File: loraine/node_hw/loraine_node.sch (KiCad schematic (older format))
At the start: 36 parts

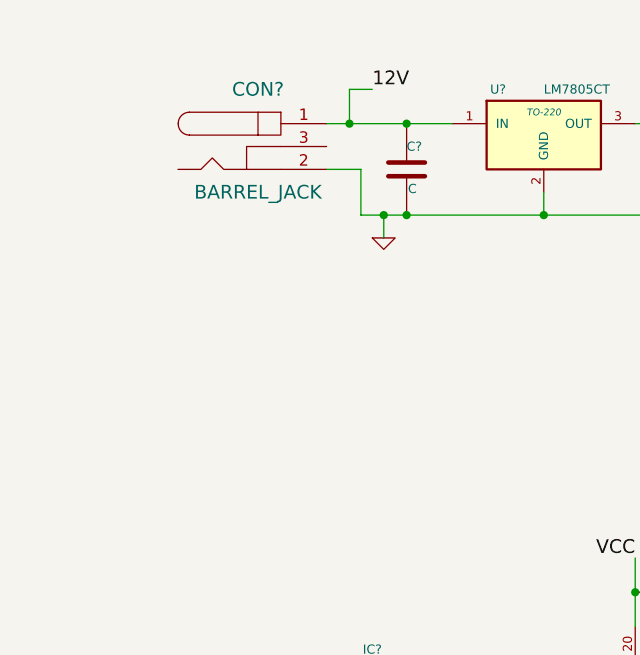
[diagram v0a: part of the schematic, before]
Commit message: Added extra power connectors
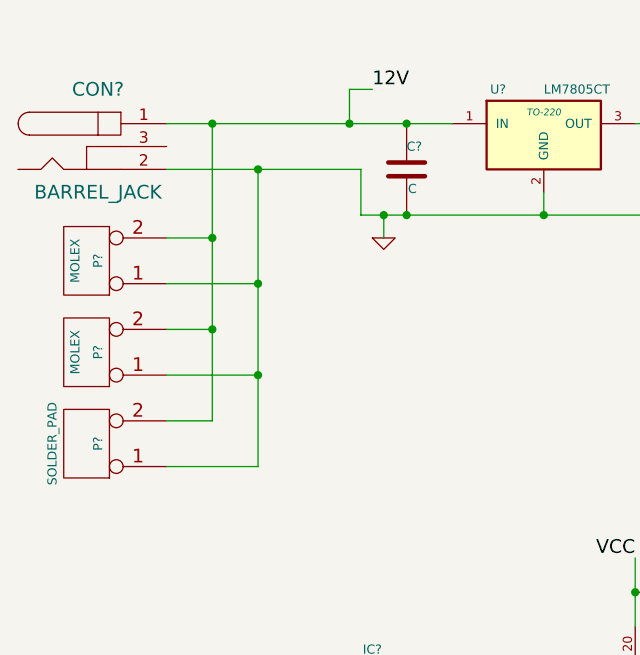
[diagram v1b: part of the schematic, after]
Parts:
- added P? (x2): MOLEX, symbol CONN_2
- added P?: SOLDER_PAD, symbol CONN_2
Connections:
- net 12V: now also P?.2 (PM), P?.2 (PM), P?.2 (PM)
- net GND: now also P?.1 (P1), P?.1 (P1), P?.1 (P1)
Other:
- moved on the sheet: CON?
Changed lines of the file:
@@
 L BARREL_JACK CON?
 U 1 1 533879A3
-P 1800 1250
-F 0 "CON?" H 1800 1500 60  0000 C CNN
-F 1 "BARREL_JACK" H 1800 1050 60  0000 C CNN
-F 2 "" H 1800 1250 60  0000 C CNN
-F 3 "" H 1800 1250 60  0000 C CNN
-	1    1800 1250
+P 1100 1250
+F 0 "CON?" H 1100 1500 60  0000 C CNN
+F 1 "BARREL_JACK" H 1100 1050 60  0000 C CNN
+F 2 "" H 1100 1250 60  0000 C CNN
+F 3 "" H 1100 1250 60  0000 C CNN
+	1    1100 1250
 	1    0    0    -1
 $EndComp
@@
 	3450 1150 4150 1150
 Wire Wire Line
-	2100 1150 2650 1150
-Wire Wire Line
-	2100 1350 2250 1350
+	1400 1150 2650 1150
+Wire Wire Line
+	1400 1350 2250 1350
 Wire Wire Line
 	2250 1350 2250 1550
@@
 Wire Wire Line
 	3850 3200 3850 3350
+$Comp
+L CONN_2 P?
+U 1 1 5338B71A
+P 1050 1750
+F 0 "P?" V 1000 1750 40  0000 C CNN
+F 1 "MOLEX" V 1100 1750 40  0000 C CNN
+F 2 "" H 1050 1750 60  0000 C CNN
+F 3 "" H 1050 1750 60  0000 C CNN
+	1    1050 1750
+	-1   0    0    1
+$EndComp
+$Comp
+L CONN_2 P?
+U 1 1 5338B738
+P 1050 2150
+F 0 "P?" V 1000 2150 40  0000 C CNN
+F 1 "MOLEX" V 1100 2150 40  0000 C CNN
+F 2 "" H 1050 2150 60  0000 C CNN
+F 3 "" H 1050 2150 60  0000 C CNN
+	1    1050 2150
+	-1   0    0    1
+$EndComp
+Wire Wire Line
+	1600 1150 1600 2450
+Connection ~ 1600 1150
+Wire Wire Line
+	1600 2050 1400 2050
+Wire Wire Line
+	1400 1650 1600 1650
+Connection ~ 1600 1650
+Wire Wire Line
+	1400 1850 1800 1850
+Wire Wire Line
+	1800 1350 1800 2650
+Connection ~ 1800 1350
+Wire Wire Line
+	1800 2250 1400 2250
+Connection ~ 1800 1850
+$Comp
+L CONN_2 P?
+U 1 1 5338BC50
+P 1050 2550
+F 0 "P?" V 1000 2550 40  0000 C CNN
+F 1 "SOLDER_PAD" V 1200 2550 40  0000 C CNN
+F 2 "" H 1050 2550 60  0000 C CNN
+F 3 "" H 1050 2550 60  0000 C CNN
+	1    1050 2550
+	-1   0    0    1
+$EndComp
+Wire Wire Line
+	1600 2450 1400 2450
+Connection ~ 1600 2050
+Wire Wire Line
+	1800 2650 1400 2650
+Connection ~ 1800 2250
 $EndSCHEMATC

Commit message: Added ICSP header
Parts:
- added P?: ICSP, symbol CONN_3X2
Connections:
- net GND: now also P?.6
- net VCC: now also P?.2
- net RESET: now reaches IC?.1 (PA2(~RESET~/dW/PCINT10))
- net RESET: now also P?.5
- net MOSI: now reaches IC?.17 ((PCINT5/MOSI/DI/SDA)PB5), R?.2
- net MOSI: now also P?.4
- net MISO: now reaches IC?.18 ((PCINT6/MISO/DO)PB6), R?.2
- net MISO: now also P?.1
- net SCK: now reaches IC?.19 ((PCINT7/USCK/SCK/SCL)PB7), R?.2
- net SCK: now also P?.3
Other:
- moved on the sheet: D?, P?, Q?, R?

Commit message: Added common anodes to outputs connector
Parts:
- removed P?: CONN_8, symbol CONN_8
- added P?: OUTPUTS, symbol CONN_8X2
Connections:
- net 12V: now also P?.10, P?.12, P?.14, P?.16, P?.2, P?.4, P?.6, P?.8
- net at D?.2 (K), Q?.3: now also P?.1
- net at D?.2 (K), Q?.3: now also P?.3
- net at D?.2 (K), Q?.3: now also P?.5
- net at Q?.3: now also P?.7
- net at Q?.3: now also P?.9
- net at Q?.3: now also P?.11
- net at Q?.3: now also P?.13
- net at Q?.3: now also P?.15
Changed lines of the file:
@@
 $EndComp
 Connection ~ 7000 6000
-$Comp
-L CONN_8 P?
-U 1 1 533887C0
-P 10950 5250
-F 0 "P?" V 10900 5250 60  0000 C CNN
-F 1 "CONN_8" V 11000 5250 60  0000 C CNN
-F 2 "" H 10950 5250 60  0000 C CNN
-F 3 "" H 10950 5250 60  0000 C CNN
-	1    10950 5250
-	1    0    0    -1
-$EndComp
 Text Label 3450 3050 2    60   ~ 0
 VCC
@@
 	3000 7150 3200 7150
 Wire Wire Line
-	6900 5600 10600 5600
-Wire Wire Line
-	7350 5500 10600 5500
-Wire Wire Line
-	7450 5400 10600 5400
-Wire Wire Line
 	6900 5100 7350 5100
 Wire Wire Line
-	7350 5100 7350 5500
-Wire Wire Line
-	7450 5400 7450 4600
-Wire Wire Line
 	7450 4600 6900 4600
 Wire Wire Line
@@
 Wire Wire Line
 	7950 2100 7950 4900
-Wire Wire Line
-	7550 5300 10600 5300
-Wire Wire Line
-	7650 5200 10600 5200
-Wire Wire Line
-	7750 5100 10600 5100
-Wire Wire Line
-	7850 5000 10600 5000
-Wire Wire Line
-	7950 4900 10600 4900
 $Comp
 L LED D?
@@
 Wire Wire Line
 	1950 3650 2100 3650
+$Comp
+L CONN_8X2 P?
+U 1 1 5338D875
+P 10050 5250
+F 0 "P?" H 10050 5700 60  0000 C CNN
+F 1 "OUTPUTS" V 10050 5250 50  0000 C CNN
+F 2 "" H 10050 5250 60  0000 C CNN
+F 3 "" H 10050 5250 60  0000 C CNN
+	1    10050 5250
+	1    0    0    -1
+$EndComp
+Wire Wire Line
+	6900 5600 9650 5600
+Wire Wire Line
+	7350 5100 7350 5500
+Wire Wire Line
+	7350 5500 9650 5500
+Wire Wire Line
+	7450 4600 7450 5400
+Wire Wire Line
+	7450 5400 9650 5400
+Wire Wire Line
+	7550 5300 9650 5300
+Wire Wire Line
+	7650 5200 9650 5200
+Wire Wire Line
+	7750 5100 9650 5100
+Wire Wire Line
+	7850 5000 9650 5000
+Wire Wire Line
+	7950 4900 9650 4900
+Text Label 10600 4800 0    60   ~ 0
+12V
+Wire Wire Line
+	10600 4800 10600 5600
+Wire Wire Line
+	10600 4900 10450 4900
+Wire Wire Line
+	10600 5000 10450 5000
+Connection ~ 10600 4900
+Wire Wire Line
+	10600 5100 10450 5100
+Connection ~ 10600 5000
+Wire Wire Line
+	10600 5200 10450 5200
+Connection ~ 10600 5100
+Wire Wire Line
+	10600 5300 10450 5300
+Connection ~ 10600 5200
+Wire Wire Line
+	10600 5400 10450 5400
+Connection ~ 10600 5300
+Wire Wire Line
+	10450 5500 10600 5500
+Connection ~ 10600 5400
+Wire Wire Line
+	10600 5600 10450 5600
+Connection ~ 10600 5500
 $EndSCHEMATC

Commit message: Filled in most component values
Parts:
- removed C? (x2): C, symbol C
- added C?: 0.33uF, symbol CP1
- C? (x2): value C -> 16pF
- C?: value CP1 -> 0.1uF
- C? (x2): value C -> 0.1u
- D?: value LED -> RED
- D?: value LED -> GREEN
- D?: value LED -> BLUE
- P?: value CONN_2 -> BUS
- R? (x8): value R -> 1k
- U?: value LM7805CT -> UA7805CKCT
- X?: value CRYSTAL -> 16MHz
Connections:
- net 12V: now also C?.1
- net GND: now also C?.2
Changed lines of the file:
@@
 P 3050 1200
 F 0 "U?" H 2850 1400 40  0000 C CNN
-F 1 "LM7805CT" H 3050 1400 40  0000 L CNN
+F 1 "UA7805CKCT" H 3050 1400 40  0000 L CNN
 F 2 "TO-220" H 3050 1300 30  0000 C CIN
 F 3 "" H 3050 1200 60  0000 C CNN
@@
 P 1800 4250
 F 0 "X?" H 1800 4400 60  0000 C CNN
-F 1 "CRYSTAL" H 1800 4100 60  0000 C CNN
+F 1 "16MHz" H 1800 4100 60  0000 C CNN
 F 2 "" H 1800 4250 60  0000 C CNN
 F 3 "" H 1800 4250 60  0000 C CNN
@@
 P 5850 3650
 F 0 "R?" V 5800 3850 40  0000 C CNN
-F 1 "R" V 5857 3651 40  0000 C CNN
+F 1 "1k" V 5857 3651 40  0000 C CNN
 F 2 "" V 5780 3650 30  0000 C CNN
 F 3 "" H 5850 3650 30  0000 C CNN
@@
 P 1450 4550
 F 0 "C?" H 1450 4650 40  0000 L CNN
-F 1 "C" H 1456 4465 40  0000 L CNN
+F 1 "16pF" H 1456 4465 40  0000 L CNN
 F 2 "" H 1488 4400 30  0000 C CNN
 F 3 "" H 1450 4550 60  0000 C CNN
@@
 P 1450 3950
 F 0 "C?" H 1450 4050 40  0000 L CNN
-F 1 "C" H 1456 3865 40  0000 L CNN
+F 1 "16pF" H 1456 3865 40  0000 L CNN
 F 2 "" H 1488 3800 30  0000 C CNN
 F 3 "" H 1450 3950 60  0000 C CNN
@@
 Text Label 2300 1000 0    60   ~ 0
 12V
-Text Label 4150 1550 0    60   ~ 0
+Text Label 3850 1550 0    60   ~ 0
 GND
 $Comp
@@
 	1    0    0    -1
 $EndComp
-Text Label 4150 1150 0    60   ~ 0
+Text Label 3850 1150 0    60   ~ 0
 VCC
-$Comp
-L C C?
-U 1 1 53387A28
-P 2450 1350
-F 0 "C?" H 2450 1450 40  0000 L CNN
-F 1 "C" H 2456 1265 40  0000 L CNN
-F 2 "" H 2488 1200 30  0000 C CNN
-F 3 "" H 2450 1350 60  0000 C CNN
-	1    2450 1350
-	1    0    0    -1
-$EndComp
 $Comp
 L CP1 C?
@@
 P 3600 1350
 F 0 "C?" H 3650 1450 50  0000 L CNN
-F 1 "CP1" H 3650 1250 50  0000 L CNN
+F 1 "0.1uF" H 3650 1250 50  0000 L CNN
 F 2 "" H 3600 1350 60  0000 C CNN
 F 3 "" H 3600 1350 60  0000 C CNN
@@
 	1    0    0    -1
 $EndComp
-Connection ~ 2450 1150
 Wire Wire Line
 	3050 1550 3050 1450
-Connection ~ 2450 1550
 Wire Wire Line
 	2350 1550 2350 1650
@@
 Connection ~ 3600 1150
 Connection ~ 3050 1550
-$Comp
-L C C?
-U 1 1 53387D68
-P 3900 1350
-F 0 "C?" H 3900 1450 40  0000 L CNN
-F 1 "C" H 3906 1265 40  0000 L CNN
-F 2 "" H 3938 1200 30  0000 C CNN
-F 3 "" H 3900 1350 60  0000 C CNN
-	1    3900 1350
-	1    0    0    -1
-$EndComp
-Connection ~ 3900 1150
 Connection ~ 3600 1550
-Wire Wire Line
-	2250 1550 4150 1550
-Connection ~ 3900 1550
-Wire Wire Line
-	3450 1150 4150 1150
-Wire Wire Line
-	1400 1150 2650 1150
 Wire Wire Line
 	1400 1350 2250 1350
@@
 P 5850 3750
 F 0 "R?" V 5800 3950 40  0000 C CNN
-F 1 "R" V 5857 3751 40  0000 C CNN
+F 1 "1k" V 5857 3751 40  0000 C CNN
 F 2 "" V 5780 3750 30  0000 C CNN
 F 3 "" H 5850 3750 30  0000 C CNN
@@
 P 5850 3850
 F 0 "R?" V 5800 4050 40  0000 C CNN
-F 1 "R" V 5857 3851 40  0000 C CNN
+F 1 "1k" V 5857 3851 40  0000 C CNN
 F 2 "" V 5780 3850 30  0000 C CNN
 F 3 "" H 5850 3850 30  0000 C CNN
@@
 P 5850 3950
 F 0 "R?" V 5800 4150 40  0000 C CNN
-F 1 "R" V 5857 3951 40  0000 C CNN
+F 1 "1k" V 5857 3951 40  0000 C CNN
 F 2 "" V 5780 3950 30  0000 C CNN
 F 3 "" H 5850 3950 30  0000 C CNN
@@
 P 5850 4050
 F 0 "R?" V 5800 4250 40  0000 C CNN
-F 1 "R" V 5857 4051 40  0000 C CNN
+F 1 "1k" V 5857 4051 40  0000 C CNN
 F 2 "" V 5780 4050 30  0000 C CNN
 F 3 "" H 5850 4050 30  0000 C CNN
@@
 P 5850 4150
 F 0 "R?" V 5800 4350 40  0000 C CNN
-F 1 "R" V 5857 4151 40  0000 C CNN
+F 1 "1k" V 5857 4151 40  0000 C CNN
 F 2 "" V 5780 4150 30  0000 C CNN
 F 3 "" H 5850 4150 30  0000 C CNN
@@
 P 5850 4250
 F 0 "R?" V 5800 4450 40  0000 C CNN
-F 1 "R" V 5857 4251 40  0000 C CNN
+F 1 "1k" V 5857 4251 40  0000 C CNN
 F 2 "" V 5780 4250 30  0000 C CNN
 F 3 "" H 5850 4250 30  0000 C CNN
@@
 P 5850 4350
 F 0 "R?" V 5800 4550 40  0000 C CNN
-F 1 "R" V 5857 4351 40  0000 C CNN
+F 1 "1k" V 5857 4351 40  0000 C CNN
 F 2 "" V 5780 4350 30  0000 C CNN
 F 3 "" H 5850 4350 30  0000 C CNN
@@
 Text Label 3450 3050 2    60   ~ 0
 VCC
-Text Label 3650 5450 2    60   ~ 0
-GND
 $Comp
 L ATTINY2313A-S IC?
@@
 $EndComp
 Wire Wire Line
-	3450 5450 3650 5450
-Wire Wire Line
 	4450 7000 4750 7000
 Wire Wire Line
@@
 P 2650 7050
 F 0 "P?" V 2600 7050 40  0000 C CNN
-F 1 "CONN_2" V 2700 7050 40  0000 C CNN
+F 1 "BUS" V 2700 7050 40  0000 C CNN
 F 2 "" H 2650 7050 60  0000 C CNN
 F 3 "" H 2650 7050 60  0000 C CNN
@@
 P 9050 1800
 F 0 "D?" H 9050 1900 50  0000 C CNN
-F 1 "LED" H 9050 1700 50  0000 C CNN
+F 1 "RED" H 9050 1700 50  0000 C CNN
 F 2 "" H 9050 1800 60  0000 C CNN
 F 3 "" H 9050 1800 60  0000 C CNN
@@
 P 9450 1800
 F 0 "D?" H 9450 1900 50  0000 C CNN
-F 1 "LED" H 9450 1700 50  0000 C CNN
+F 1 "GREEN" H 9400 1700 50  0000 C CNN
 F 2 "" H 9450 1800 60  0000 C CNN
 F 3 "" H 9450 1800 60  0000 C CNN
@@
 P 9850 1800
 F 0 "D?" H 9850 1900 50  0000 C CNN
-F 1 "LED" H 9850 1700 50  0000 C CNN
+F 1 "BLUE" H 9850 1700 50  0000 C CNN
 F 2 "" H 9850 1800 60  0000 C CNN
 F 3 "" H 9850 1800 60  0000 C CNN
@@
 U 1 1 5338A896
 P 2300 7050
-F 0 "C?" H 2300 7150 40  0000 L CNN
-F 1 "C" H 2306 6965 40  0000 L CNN
+F 0 "C?" H 2350 7150 40  0000 L CNN
+F 1 "0.1u" H 2340 6950 40  0000 L CNN
 F 2 "" H 2338 6900 30  0000 C CNN
 F 3 "" H 2300 7050 60  0000 C CNN
@@
 U 1 1 5338AB56
 P 3650 3200
-F 0 "C?" H 3650 3300 40  0000 L CNN
-F 1 "C" H 3656 3115 40  0000 L CNN
+F 0 "C?" V 3600 3250 40  0000 L CNN
+F 1 "0.1u" V 3710 3020 40  0000 L CNN
 F 2 "" H 3688 3050 30  0000 C CNN
 F 3 "" H 3650 3200 60  0000 C CNN
@@
 	10600 5600 10450 5600
 Connection ~ 10600 5500
+$Comp
+L CP1 C?
+U 1 1 5338EB5B
+P 2450 1350
+F 0 "C?" H 2500 1450 50  0000 L CNN
+F 1 "0.33uF" H 2500 1250 50  0000 L CNN
+F 2 "" H 2450 1350 60  0000 C CNN
+F 3 "" H 2450 1350 60  0000 C CNN
+	1    2450 1350
+	1    0    0    -1
+$EndComp
+Wire Wire Line
+	1400 1150 2650 1150
+Connection ~ 2450 1150
+Connection ~ 2450 1550
+Wire Wire Line
+	2250 1550 3850 1550
+Wire Wire Line
+	3450 1150 3850 1150
+$Comp
+L GND #PWR?
+U 1 1 5338F7A1
+P 3450 5500
+F 0 "#PWR?" H 3450 5500 30  0001 C CNN
+F 1 "GND" H 3450 5430 30  0001 C CNN
+F 2 "" H 3450 5500 60  0000 C CNN
+F 3 "" H 3450 5500 60  0000 C CNN
+	1    3450 5500
+	1    0    0    -1
+$EndComp
+Wire Wire Line
+	3450 5450 3450 5500
 $EndSCHEMATC

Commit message: Replaced VCC/GND labels with symbols
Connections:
- net VCC: no longer R?.1, R?.1, R?.1
- net 12V renamed +12V
- net +12V: now also R?.1, R?.1, R?.1
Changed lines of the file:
@@
 	1    0    0    -1
 $EndComp
-Text Label 2300 1000 0    60   ~ 0
-12V
-Text Label 3850 1550 0    60   ~ 0
-GND
 $Comp
 L GND #PWR?
 U 1 1 533879F1
-P 2350 1650
-F 0 "#PWR?" H 2350 1650 30  0001 C CNN
-F 1 "GND" H 2350 1580 30  0001 C CNN
-F 2 "" H 2350 1650 60  0000 C CNN
-F 3 "" H 2350 1650 60  0000 C CNN
-	1    2350 1650
-	1    0    0    -1
-$EndComp
-Text Label 3850 1150 0    60   ~ 0
-VCC
+P 3850 1650
+F 0 "#PWR?" H 3850 1650 30  0001 C CNN
+F 1 "GND" H 3850 1580 30  0001 C CNN
+F 2 "" H 3850 1650 60  0000 C CNN
+F 3 "" H 3850 1650 60  0000 C CNN
+	1    3850 1650
+	1    0    0    -1
+$EndComp
 $Comp
 L CP1 C?
@@
 Wire Wire Line
 	3050 1550 3050 1450
-Wire Wire Line
-	2350 1550 2350 1650
-Connection ~ 2350 1550
 Connection ~ 3600 1150
 Connection ~ 3050 1550
@@
 Wire Wire Line
 	2250 1350 2250 1550
-Wire Wire Line
-	2200 1000 2300 1000
 Connection ~ 2200 1150
-Wire Wire Line
-	2200 1150 2200 1000
 $Comp
 L R R?
@@
 $EndComp
 Connection ~ 7000 6000
-Text Label 3450 3050 2    60   ~ 0
-VCC
 $Comp
 L ATTINY2313A-S IC?
@@
 Wire Wire Line
 	5100 6850 4450 6850
-Text Label 2200 6850 2    60   ~ 0
-VCC
-Wire Wire Line
-	2200 7300 3200 7300
-Text Label 2200 7300 2    60   ~ 0
-GND
 $Comp
 L CONN_2 P?
@@
 	9850 3100 9850 2000
 Connection ~ 7750 3100
-Text Label 8750 800  2    60   ~ 0
-VCC
 Wire Wire Line
 	9050 800  9050 1000
@@
 Wire Wire Line
 	9850 1500 9850 1600
-Wire Wire Line
-	2200 6850 3200 6850
 $Comp
 L C C?
@@
 Connection ~ 2300 6850
 Wire Wire Line
-	2300 7300 2300 7250
+	2300 7250 2300 7350
 Connection ~ 2300 7300
 $Comp
@@
 	1    0    0    -1
 $EndComp
-Wire Wire Line
-	3450 3050 3450 3350
 Connection ~ 3450 3200
 Wire Wire Line
@@
 Wire Wire Line
 	7950 4900 9650 4900
-Text Label 10600 4800 0    60   ~ 0
-12V
 Wire Wire Line
 	10600 4800 10600 5600
@@
 Wire Wire Line
 	3450 5450 3450 5500
+Wire Wire Line
+	3850 1550 3850 1650
+$Comp
+L GND #PWR?
+U 1 1 5338FB33
+P 5700 3050
+F 0 "#PWR?" H 5700 3050 30  0001 C CNN
+F 1 "GND" H 5700 2980 30  0001 C CNN
+F 2 "" H 5700 3050 60  0000 C CNN
+F 3 "" H 5700 3050 60  0000 C CNN
+	1    5700 3050
+	1    0    0    -1
+$EndComp
+Wire Wire Line
+	5700 3000 5700 3050
+$Comp
+L GND #PWR?
+U 1 1 5338FCA4
+P 2300 7350
+F 0 "#PWR?" H 2300 7350 30  0001 C CNN
+F 1 "GND" H 2300 7280 30  0001 C CNN
+F 2 "" H 2300 7350 60  0000 C CNN
+F 3 "" H 2300 7350 60  0000 C CNN
+	1    2300 7350
+	1    0    0    -1
+$EndComp
+Wire Wire Line
+	3200 7300 2300 7300
+$Comp
+L +12V #PWR?
+U 1 1 5339006C
+P 2200 1100
+F 0 "#PWR?" H 2200 1050 20  0001 C CNN
+F 1 "+12V" H 2200 1200 30  0000 C CNN
+F 2 "" H 2200 1100 60  0000 C CNN
+F 3 "" H 2200 1100 60  0000 C CNN
+	1    2200 1100
+	1    0    0    -1
+$EndComp
+$Comp
+L VCC #PWR?
+U 1 1 53390080
+P 3850 1100
+F 0 "#PWR?" H 3850 1200 30  0001 C CNN
+F 1 "VCC" H 3850 1200 30  0000 C CNN
+F 2 "" H 3850 1100 60  0000 C CNN
+F 3 "" H 3850 1100 60  0000 C CNN
+	1    3850 1100
+	1    0    0    -1
+$EndComp
+Wire Wire Line
+	3850 1150 3850 1100
+Wire Wire Line
+	2200 1100 2200 1150
+Wire Wire Line
+	3450 3350 3450 3150
+$Comp
+L VCC #PWR?
+U 1 1 53390544
+P 3450 3150
+F 0 "#PWR?" H 3450 3250 30  0001 C CNN
+F 1 "VCC" H 3450 3250 30  0000 C CNN
+F 2 "" H 3450 3150 60  0000 C CNN
+F 3 "" H 3450 3150 60  0000 C CNN
+	1    3450 3150
+	1    0    0    -1
+$EndComp
+$Comp
+L VCC #PWR?
+U 1 1 5339060A
+P 5600 2750
+F 0 "#PWR?" H 5600 2850 30  0001 C CNN
+F 1 "VCC" H 5600 2850 30  0000 C CNN
+F 2 "" H 5600 2750 60  0000 C CNN
+F 3 "" H 5600 2750 60  0000 C CNN
+	1    5600 2750
+	1    0    0    -1
+$EndComp
+Wire Wire Line
+	5600 2800 5600 2750
+Connection ~ 5600 2800
+$Comp
+L +12V #PWR?
+U 1 1 533907F9
+P 8750 800
+F 0 "#PWR?" H 8750 750 20  0001 C CNN
+F 1 "+12V" H 8750 900 30  0000 C CNN
+F 2 "" H 8750 800 60  0000 C CNN
+F 3 "" H 8750 800 60  0000 C CNN
+	1    8750 800
+	1    0    0    -1
+$EndComp
+$Comp
+L VCC #PWR?
+U 1 1 5339091E
+P 2300 6800
+F 0 "#PWR?" H 2300 6900 30  0001 C CNN
+F 1 "VCC" H 2300 6900 30  0000 C CNN
+F 2 "" H 2300 6800 60  0000 C CNN
+F 3 "" H 2300 6800 60  0000 C CNN
+	1    2300 6800
+	1    0    0    -1
+$EndComp
+Wire Wire Line
+	2300 6850 2300 6800
+Wire Wire Line
+	2300 6850 3200 6850
+$Comp
+L +12V #PWR?
+U 1 1 53390BA6
+P 10600 4800
+F 0 "#PWR?" H 10600 4750 20  0001 C CNN
+F 1 "+12V" H 10600 4900 30  0000 C CNN
+F 2 "" H 10600 4800 60  0000 C CNN
+F 3 "" H 10600 4800 60  0000 C CNN
+	1    10600 4800
+	1    0    0    -1
+$EndComp
 $EndSCHEMATC

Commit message: Specced darlington drivers
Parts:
- Q? (x8): value DARL_N -> FZT600
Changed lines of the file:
@@
 P 6750 2350
 F 0 "Q?" H 6750 2600 50  0000 C CNN
-F 1 "DARL_N" H 6650 2250 50  0000 C CNN
+F 1 "FZT600" H 6650 2250 50  0000 C CNN
 F 2 "" H 6750 2350 60  0000 C CNN
 F 3 "" H 6750 2350 60  0000 C CNN
@@
 P 6750 2850
 F 0 "Q?" H 6750 3100 50  0000 C CNN
-F 1 "DARL_N" H 6650 2750 50  0000 C CNN
+F 1 "FZT600" H 6650 2750 50  0000 C CNN
 F 2 "" H 6750 2850 60  0000 C CNN
 F 3 "" H 6750 2850 60  0000 C CNN
@@
 P 6750 3350
 F 0 "Q?" H 6750 3600 50  0000 C CNN
-F 1 "DARL_N" H 6650 3250 50  0000 C CNN
+F 1 "FZT600" H 6650 3250 50  0000 C CNN
 F 2 "" H 6750 3350 60  0000 C CNN
 F 3 "" H 6750 3350 60  0000 C CNN
@@
 P 6750 3850
 F 0 "Q?" H 6750 4100 50  0000 C CNN
-F 1 "DARL_N" H 6650 3750 50  0000 C CNN
+F 1 "FZT600" H 6650 3750 50  0000 C CNN
 F 2 "" H 6750 3850 60  0000 C CNN
 F 3 "" H 6750 3850 60  0000 C CNN
@@
 P 6750 4350
 F 0 "Q?" H 6750 4600 50  0000 C CNN
-F 1 "DARL_N" H 6650 4250 50  0000 C CNN
+F 1 "FZT600" H 6650 4250 50  0000 C CNN
 F 2 "" H 6750 4350 60  0000 C CNN
 F 3 "" H 6750 4350 60  0000 C CNN
@@
 P 6750 4850
 F 0 "Q?" H 6750 5100 50  0000 C CNN
-F 1 "DARL_N" H 6650 4750 50  0000 C CNN
+F 1 "FZT600" H 6650 4750 50  0000 C CNN
 F 2 "" H 6750 4850 60  0000 C CNN
 F 3 "" H 6750 4850 60  0000 C CNN
@@
 P 6750 5350
 F 0 "Q?" H 6750 5600 50  0000 C CNN
-F 1 "DARL_N" H 6650 5250 50  0000 C CNN
+F 1 "FZT600" H 6650 5250 50  0000 C CNN
 F 2 "" H 6750 5350 60  0000 C CNN
 F 3 "" H 6750 5350 60  0000 C CNN
@@
 P 6750 5850
 F 0 "Q?" H 6750 6100 50  0000 C CNN
-F 1 "DARL_N" H 6650 5750 50  0000 C CNN
+F 1 "FZT600" H 6650 5750 50  0000 C CNN
 F 2 "" H 6750 5850 60  0000 C CNN
 F 3 "" H 6750 5850 60  0000 C CNN

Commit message: Initial netlist and most parts
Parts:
- gave numbers to parts that had none: 39
